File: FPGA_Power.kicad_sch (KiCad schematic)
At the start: 29 parts

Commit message: Made PCB mockup
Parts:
- gave numbers to parts that had none: 29

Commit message: Added loclib
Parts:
- C100, C101, C102, C103, C104, C105, C106, C91, C92, C93, C94, C95, C96, C97, C98, C99: footprint antmicro-footprints:0603-cap -> crosslink-nx-video-converter-footprints:0603-cap; symbol antmicroCapacitors0603:C_100n_0603 -> crosslink-nx-video-converter:C_100n_0603
- C84, C85, C86, C87, C88, C90: footprint antmicro-footprints:0603-cap -> crosslink-nx-video-converter-footprints:0603-cap; symbol antmicroCapacitors0603:C_10u_0603 -> crosslink-nx-video-converter:C_10u_0603
- C89: footprint antmicro-footprints:0603-cap -> crosslink-nx-video-converter-footprints:0603-cap; symbol antmicroCapacitors0603:C_1u_0603 -> crosslink-nx-video-converter:C_1u_0603
- FB1, FB2, FB3, FB4, FB5: footprint antmicro-footprints:0603-res -> crosslink-nx-video-converter-footprints:0603-res; symbol antmicroFerriteBeadsandChips:BLM18PG121SN1D -> crosslink-nx-video-converter:BLM18PG121SN1D
- U11: footprint antmicro-footprints:BGA-256_16x16_14.0x14.0mm -> crosslink-nx-video-converter-footprints:BGA-256_16x16_14.0x14.0mm; symbol antmicroBGAchips:LIFCL-40-9BG256C -> crosslink-nx-video-converter:LIFCL-40-9BG256C

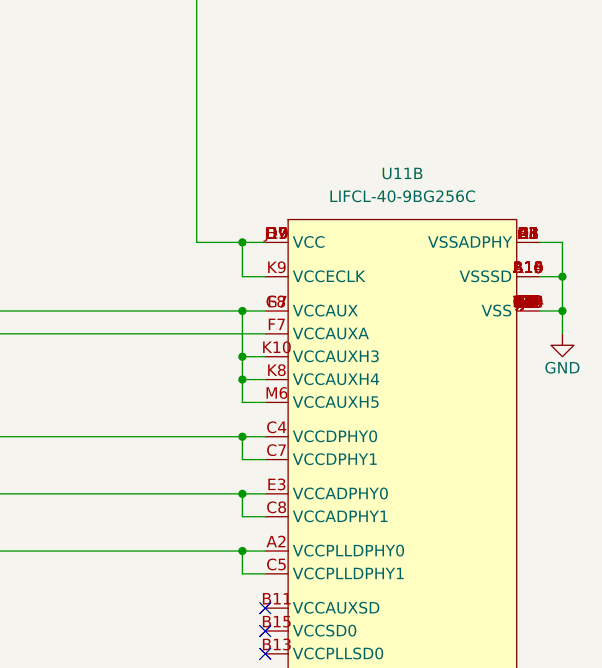
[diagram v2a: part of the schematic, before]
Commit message: Divided FPGA into multiple blocks
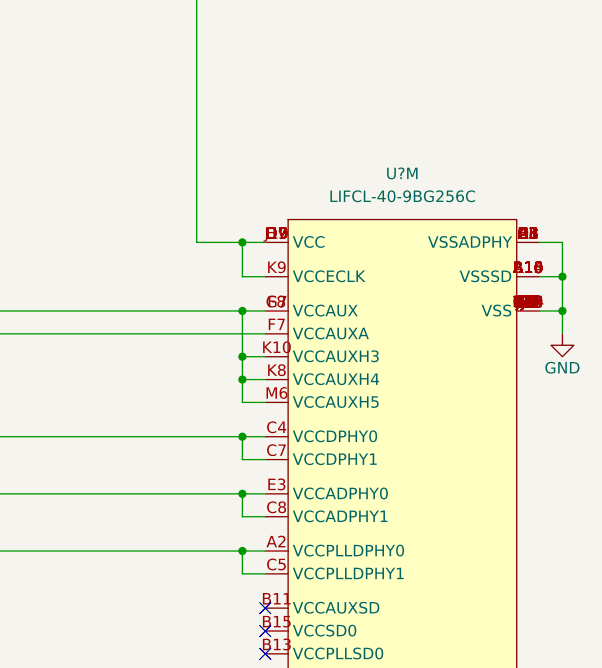
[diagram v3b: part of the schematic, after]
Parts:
- removed U11: LIFCL-40-9BG256C, crosslink-nx-video-converter-footprints:BGA-256_16x16_14.0x14.0mm, symbol crosslink-nx-video-converter:LIFCL-40-9BG256C
- added U?: LIFCL-40-9BG256C, antmicro-footprints:BGA-256_16x16_14.0x14.0mm, symbol antmicroBGAchips:LIFCL-40-9BG256C
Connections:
- net 1V0_Power: now also U?.D7 (VCC), U?.D9 (VCC), U?.H7 (VCC), U?.J10 (VCC), U?.K9 (VCCECLK)
- net GND: now also U?.A1 (VSSADPHY), U?.A10 (VSSSD), U?.A13 (VSSSD), U?.A16 (VSSSD), U?.A8 (VSSADPHY), U?.B10 (VSSSD), U?.B14 (VSSSD), U?.B8 (VSSADPHY), U?.C10 (VSS), U?.C3 (VSSADPHY), U?.C6 (VSSADPHY), U?.C9 (VSS), U?.D14 (VSS), U?.D3 (VSSADPHY), U?.D8 (VSS), U?.E7 (VSS), U?.E8 (VSS), U?.F12 (VSS), U?.F3 (VSSADPHY), U?.G1 (VSSADPHY), U?.G2 (VSS), U?.G5 (VSS), U?.G8 (VSS), U?.H8 (VSS), U?.H9 (VSS), U?.J14 (VSS), U?.J3 (VSS), U?.J7 (VSS), U?.J8 (VSS), U?.J9 (VSS), U?.M5 (VSS), U?.N7 (VSS), U?.P13 (VSS), U?.T1 (VSS), U?.T16 (VSS)
- net VCC_ADPHY: now also U?.C8 (VCCADPHY1), U?.E3 (VCCADPHY0)
- net VCC_AUX: now also U?.F8 (VCCAUX), U?.G7 (VCCAUX), U?.K10 (VCCAUXH3), U?.K8 (VCCAUXH4), U?.M6 (VCCAUXH5)
- net VCC_AUXA: now also U?.F7 (VCCAUXA)
- net VCC_DPHY: now also U?.C4 (VCCDPHY0), U?.C7 (VCCDPHY1)
- net VCC_PLLDPHY: now also U?.A2 (VCCPLLDPHY0), U?.C5 (VCCPLLDPHY1)

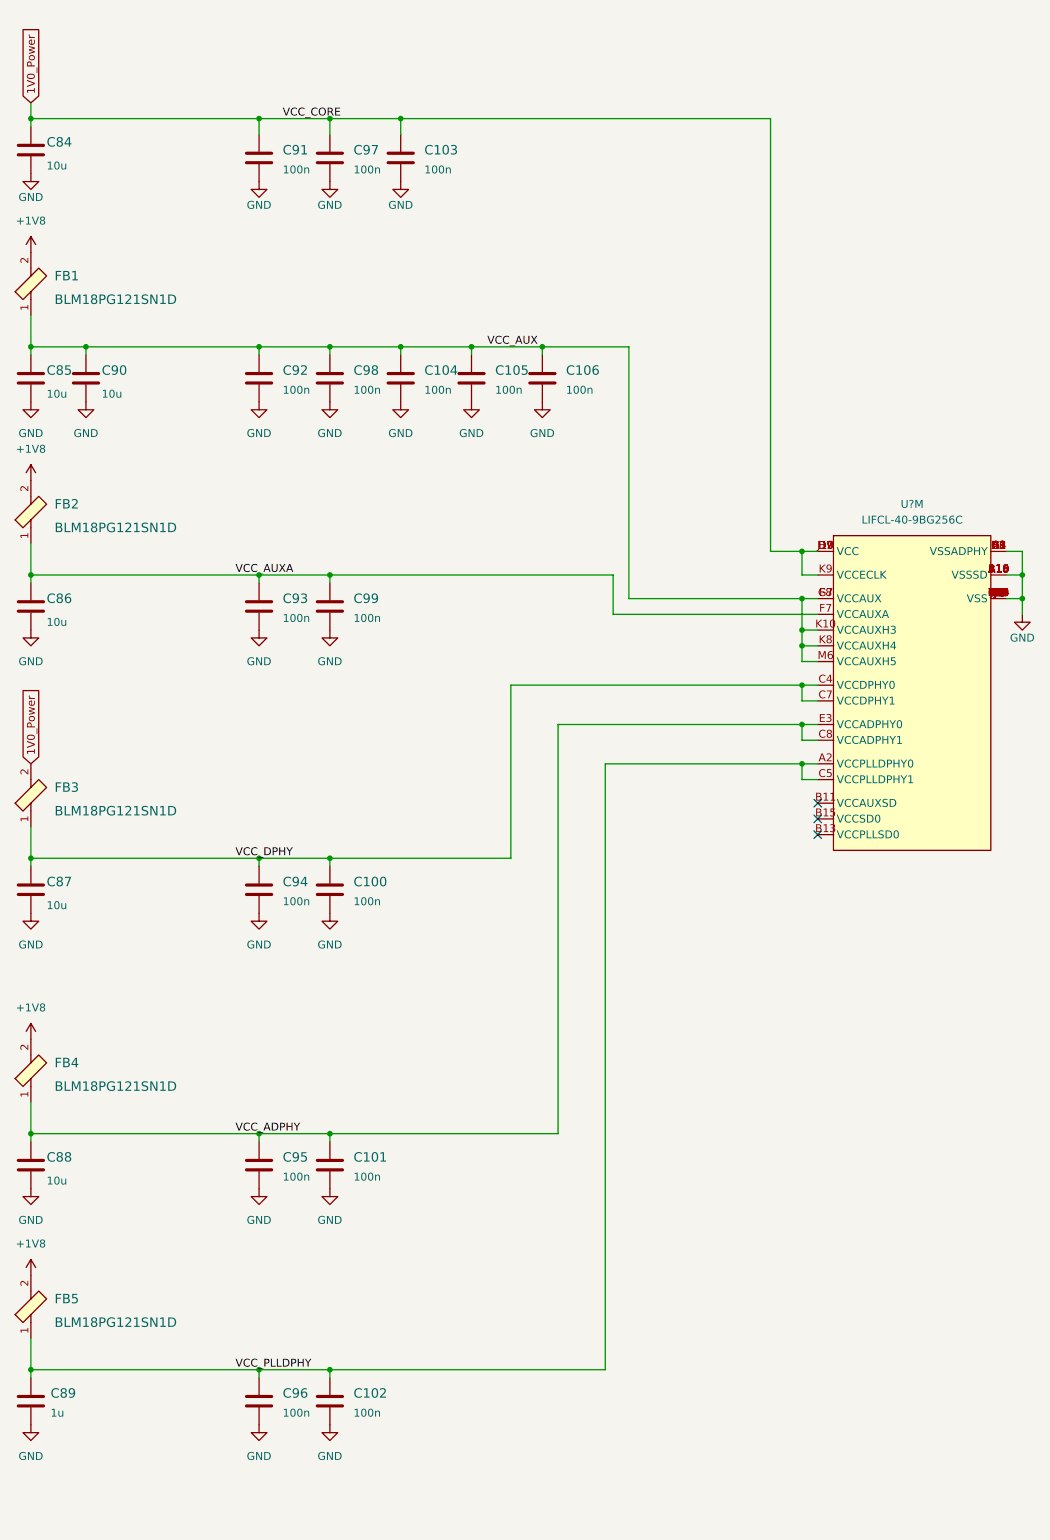
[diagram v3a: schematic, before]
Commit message: Modified power indicator and connected unused pins
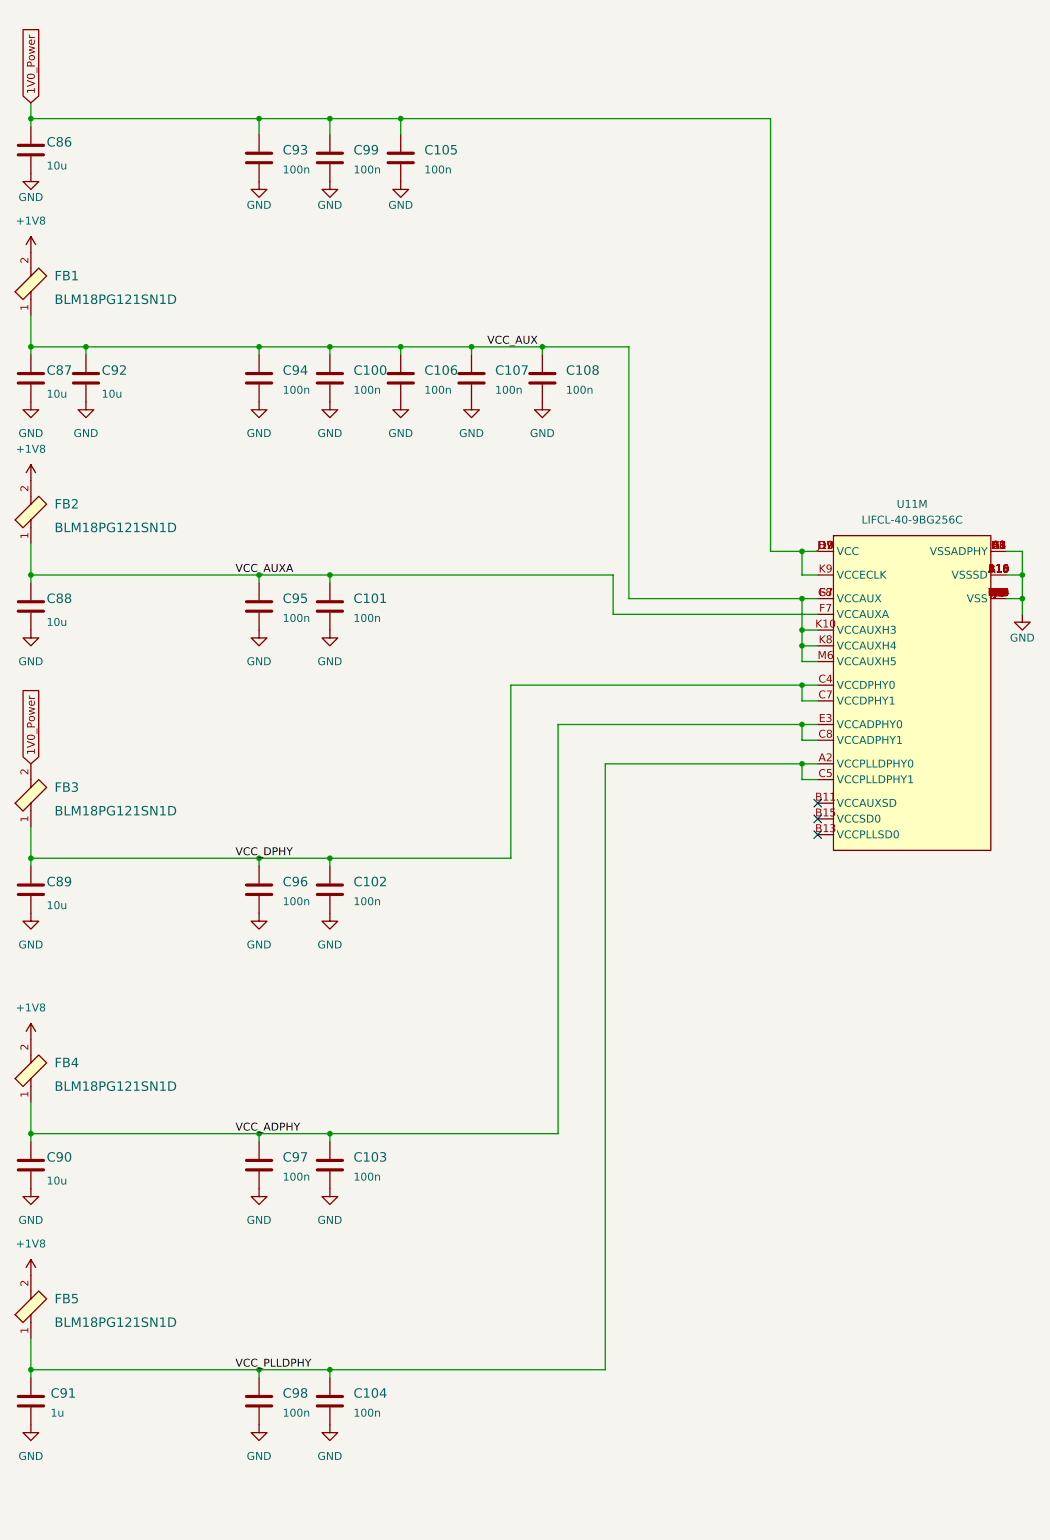
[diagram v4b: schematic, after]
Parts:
- gave numbers to parts that had none: 1
- renumbered C98 to C100, C99 to C101, C100 to C102, C101 to C103, C102 to C104, C103 to C105, C104 to C106, C105 to C107, C106 to C108, C84 to C86, C85 to C87, C86 to C88, C87 to C89, C88 to C90, C89 to C91, C90 to C92, C91 to C93, C92 to C94, C93 to C95, C94 to C96, C95 to C97, C96 to C98, C97 to C99

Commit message: Placed components
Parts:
- C100: renamed from C101; value C_100n_0603 -> C_100n_0402; footprint crosslink-nx-video-converter-footprints:0603-cap -> antmicro-footprints:0402-cap; symbol crosslink-nx-video-converter:C_100n_0603 -> antmicroCapacitors0402:C_100n_0402; MPN 0603YC104KAZ2A -> GRM155R61H104KE14D; Manufacturer AVX -> Murata
- C101: renamed from C102; value C_100n_0603 -> C_100n_0402; footprint crosslink-nx-video-converter-footprints:0603-cap -> antmicro-footprints:0402-cap; symbol crosslink-nx-video-converter:C_100n_0603 -> antmicroCapacitors0402:C_100n_0402; MPN 0603YC104KAZ2A -> GRM155R61H104KE14D; Manufacturer AVX -> Murata
- C102: renamed from C103; value C_100n_0603 -> C_100n_0402; footprint crosslink-nx-video-converter-footprints:0603-cap -> antmicro-footprints:0402-cap; symbol crosslink-nx-video-converter:C_100n_0603 -> antmicroCapacitors0402:C_100n_0402; MPN 0603YC104KAZ2A -> GRM155R61H104KE14D; Manufacturer AVX -> Murata
- C103: renamed from C104; value C_100n_0603 -> C_100n_0402; footprint crosslink-nx-video-converter-footprints:0603-cap -> antmicro-footprints:0402-cap; symbol crosslink-nx-video-converter:C_100n_0603 -> antmicroCapacitors0402:C_100n_0402; MPN 0603YC104KAZ2A -> GRM155R61H104KE14D; Manufacturer AVX -> Murata
- C104: renamed from C105; value C_100n_0603 -> C_100n_0402; footprint crosslink-nx-video-converter-footprints:0603-cap -> antmicro-footprints:0402-cap; symbol crosslink-nx-video-converter:C_100n_0603 -> antmicroCapacitors0402:C_100n_0402; MPN 0603YC104KAZ2A -> GRM155R61H104KE14D; Manufacturer AVX -> Murata
- C105: renamed from C106; value C_100n_0603 -> C_100n_0402; footprint crosslink-nx-video-converter-footprints:0603-cap -> antmicro-footprints:0402-cap; symbol crosslink-nx-video-converter:C_100n_0603 -> antmicroCapacitors0402:C_100n_0402; MPN 0603YC104KAZ2A -> GRM155R61H104KE14D; Manufacturer AVX -> Murata
- C106: renamed from C107; value C_100n_0603 -> C_100n_0402; footprint crosslink-nx-video-converter-footprints:0603-cap -> antmicro-footprints:0402-cap; symbol crosslink-nx-video-converter:C_100n_0603 -> antmicroCapacitors0402:C_100n_0402; MPN 0603YC104KAZ2A -> GRM155R61H104KE14D; Manufacturer AVX -> Murata
- C107: renamed from C108; value C_100n_0603 -> C_100n_0402; footprint crosslink-nx-video-converter-footprints:0603-cap -> antmicro-footprints:0402-cap; symbol crosslink-nx-video-converter:C_100n_0603 -> antmicroCapacitors0402:C_100n_0402; MPN 0603YC104KAZ2A -> GRM155R61H104KE14D; Manufacturer AVX -> Murata
- C85: renamed from C93; value C_100n_0603 -> C_100n_0402; footprint crosslink-nx-video-converter-footprints:0603-cap -> antmicro-footprints:0402-cap; symbol crosslink-nx-video-converter:C_100n_0603 -> antmicroCapacitors0402:C_100n_0402; MPN 0603YC104KAZ2A -> GRM155R61H104KE14D; Manufacturer AVX -> Murata
- C93: renamed from C94; value C_100n_0603 -> C_100n_0402; footprint crosslink-nx-video-converter-footprints:0603-cap -> antmicro-footprints:0402-cap; symbol crosslink-nx-video-converter:C_100n_0603 -> antmicroCapacitors0402:C_100n_0402; MPN 0603YC104KAZ2A -> GRM155R61H104KE14D; Manufacturer AVX -> Murata
- C94: renamed from C95; value C_100n_0603 -> C_100n_0402; footprint crosslink-nx-video-converter-footprints:0603-cap -> antmicro-footprints:0402-cap; symbol crosslink-nx-video-converter:C_100n_0603 -> antmicroCapacitors0402:C_100n_0402; MPN 0603YC104KAZ2A -> GRM155R61H104KE14D; Manufacturer AVX -> Murata
- C95: renamed from C96; value C_100n_0603 -> C_100n_0402; footprint crosslink-nx-video-converter-footprints:0603-cap -> antmicro-footprints:0402-cap; symbol crosslink-nx-video-converter:C_100n_0603 -> antmicroCapacitors0402:C_100n_0402; MPN 0603YC104KAZ2A -> GRM155R61H104KE14D; Manufacturer AVX -> Murata
- C96: renamed from C97; value C_100n_0603 -> C_100n_0402; footprint crosslink-nx-video-converter-footprints:0603-cap -> antmicro-footprints:0402-cap; symbol crosslink-nx-video-converter:C_100n_0603 -> antmicroCapacitors0402:C_100n_0402; MPN 0603YC104KAZ2A -> GRM155R61H104KE14D; Manufacturer AVX -> Murata
- C97: renamed from C98; value C_100n_0603 -> C_100n_0402; footprint crosslink-nx-video-converter-footprints:0603-cap -> antmicro-footprints:0402-cap; symbol crosslink-nx-video-converter:C_100n_0603 -> antmicroCapacitors0402:C_100n_0402; MPN 0603YC104KAZ2A -> GRM155R61H104KE14D; Manufacturer AVX -> Murata
- C98: renamed from C99; value C_100n_0603 -> C_100n_0402; footprint crosslink-nx-video-converter-footprints:0603-cap -> antmicro-footprints:0402-cap; symbol crosslink-nx-video-converter:C_100n_0603 -> antmicroCapacitors0402:C_100n_0402; MPN 0603YC104KAZ2A -> GRM155R61H104KE14D; Manufacturer AVX -> Murata
- C99: renamed from C100; value C_100n_0603 -> C_100n_0402; footprint crosslink-nx-video-converter-footprints:0603-cap -> antmicro-footprints:0402-cap; symbol crosslink-nx-video-converter:C_100n_0603 -> antmicroCapacitors0402:C_100n_0402; MPN 0603YC104KAZ2A -> GRM155R61H104KE14D; Manufacturer AVX -> Murata

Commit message: Loclib
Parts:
- C100, C101, C102, C103, C104, C105, C106, C107, C85, C93, C94, C95, C96, C97, C98, C99: footprint antmicro-footprints:0402-cap -> crosslink-nx-video-converter-footprints:0402-cap; symbol antmicroCapacitors0402:C_100n_0402 -> crosslink-nx-video-converter:C_100n_0402
- U11: footprint antmicro-footprints:BGA-256_16x16_14.0x14.0mm -> crosslink-nx-video-converter-footprints:BGA-256_16x16_14.0x14.0mm; symbol antmicroBGAchips:LIFCL-40-9BG256C -> crosslink-nx-video-converter:LIFCL-40-9BG256C
